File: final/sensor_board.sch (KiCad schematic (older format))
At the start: 47 parts, among them J1 USB_microB_2040002-1, J2 Arduino_ICSP, J3 Conn_01x15_Male, J4 Conn_01x15_Male, J5 BT CONFIG, U1 TXS0104E, U2 FT232RL, U3 RN4871, U4 MCP1702T-5002E_CB, U5 TPS2113ADRBR, U6 US5881, U7 ATMEGA328PB-ANR, Y1 16MHz

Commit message: Fix merge conflicts
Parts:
- added C15, C16: 1µF, Capacitor_SMD:C_0603_1608Metric, symbol Device:C
- added J?: JST-PH Connector, symbol Connector_Generic:Conn_02x02_Odd_Even
- added U7: TS02CQE, Package_DIP:DIP-8_W7.62mm, symbol Analog_Switch:ADG417BN
- added U8: MCP1702T-3302E/CBCT-ND, Package_TO_SOT_SMD:SOT-23, symbol sensor_board-rescue:MCP1702T-5002E_CB-final
- J1: symbol final:USB_microB_2040002-1 -> sensor_board-rescue:USB_microB_2040002-1-final
- J2: symbol final:Arduino_ICSP -> sensor_board-rescue:Arduino_ICSP-final
- S1, S2: symbol final:SW -> sensor_board-rescue:SW-final
- U1: symbol final:TXS0104E -> sensor_board-rescue:TXS0104E-final
- U2: symbol final:FT232RL -> sensor_board-rescue:FT232RL-final
- U4: symbol final:MCP1702T-5002E_CB -> sensor_board-rescue:MCP1702T-5002E_CB-final
- U5: symbol final:TPS2113ADRBR -> sensor_board-rescue:TPS2113ADRBR-final
- U6: symbol final:US5881 -> sensor_board-rescue:US5881-final
- U7: symbol final:ATMEGA328PB-ANR -> main_board-rescue:ATMEGA328PB-ANR-final
- Y1: symbol final:Crystal -> sensor_board-rescue:Crystal-final
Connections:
- net labels added: +3.3V
- wire segments 134 -> 146
- no-connect marks 31 -> 32
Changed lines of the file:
@@
 	4200 1900 4200 1950
-Wire Wire Line
-	4200 1900 3900 1900
-Connection ~ 4200 1900
-Text Label 3900 1900 2    50   ~ 0
-VIN
 Wire Wire Line
 	2200 4600 2400 4600
@@
 	14470 7580 14620 7580
 $Comp
-L final:TPS2113ADRBR U5
+L sensor_board-rescue:TPS2113ADRBR-final U5
 U 1 1 5C6B8D23
 P 7500 2200
@@
 $EndComp
 $Comp
-L final:MCP1702T-5002E_CB U4
+L sensor_board-rescue:MCP1702T-5002E_CB-final U4
 U 1 1 5C6B8EBC
 P 4800 2000
@@
 $EndComp
 $Comp
-L final:SW S2
+L sensor_board-rescue:SW-final S2
 U 1 1 5C6B90CD
 P 7000 5300
@@
 $EndComp
 $Comp
-L final:USB_microB_2040002-1 J1
+L sensor_board-rescue:USB_microB_2040002-1-final J1
 U 1 1 5C6B9394
 P 1550 5000
@@
 $EndComp
 $Comp
-L final:Arduino_ICSP J2
+L sensor_board-rescue:Arduino_ICSP-final J2
 U 1 1 5C6B9A65
 P 14270 7480
@@
 $EndComp
 $Comp
-L final:ATMEGA328PB-ANR U7
+L main_board-rescue:ATMEGA328PB-ANR-final U7
 U 1 1 5C6C352E
 P 9800 6100
@@
 	8650 7800 8650 7850
 $Comp
-L final:FT232RL U2
+L sensor_board-rescue:FT232RL-final U2
 U 1 1 5C6CF653
 P 4500 5500
@@
 $EndComp
 $Comp
-L final:Crystal Y1
+L sensor_board-rescue:Crystal-final Y1
 U 1 1 5C6CF8B9
 P 8500 5200
@@
 $EndComp
 $Comp
-L final:SW S1
+L sensor_board-rescue:SW-final S1
 U 1 1 5CB4A3A3
 P 6710 9320
@@
 	13810 8310 14220 8310
 $Comp
-L final:TXS0104E U1
+L sensor_board-rescue:TXS0104E-final U1
 U 1 1 5CAAB751
 P 2880 9420
@@
 $EndComp
 $Comp
-L final:US5881 U6
+L sensor_board-rescue:US5881-final U6
 U 1 1 5CAB13C9
 P 8450 9120
@@
 Text Label 8800 9120 0    50   ~ 0
 D2
+$Comp
+L power:GND #PWR056
+U 1 1 5CAB55FC
+P 3500 1450
+F 0 "#PWR056" H 3500 1200 50  0001 C CNN
+F 1 "GND" H 3505 1277 50  0000 C CNN
+F 2 "" H 3500 1450 50  0001 C CNN
+F 3 "" H 3500 1450 50  0001 C CNN
+	1    3500 1450
+	1    0    0    -1
+$EndComp
+$Comp
+L Device:C C16
+U 1 1 5CAB5602
+P 4100 1150
+F 0 "C16" H 4215 1196 50  0000 L CNN
+F 1 "1µF" H 4215 1105 50  0000 L CNN
+F 2 "Capacitor_SMD:C_0603_1608Metric" H 4138 1000 50  0001 C CNN
+F 3 "~" H 4100 1150 50  0001 C CNN
+	1    4100 1150
+	1    0    0    -1
+$EndComp
+$Comp
+L power:GND #PWR057
+U 1 1 5CAB5609
+P 4100 1300
+F 0 "#PWR057" H 4100 1050 50  0001 C CNN
+F 1 "GND" H 4105 1127 50  0000 C CNN
+F 2 "" H 4100 1300 50  0001 C CNN
+F 3 "" H 4100 1300 50  0001 C CNN
+	1    4100 1300
+	1    0    0    -1
+$EndComp
+$Comp
+L Device:C C15
+U 1 1 5CAB560F
+P 2900 1150
+F 0 "C15" H 3015 1196 50  0000 L CNN
+F 1 "1µF" H 3015 1105 50  0000 L CNN
+F 2 "Capacitor_SMD:C_0603_1608Metric" H 2938 1000 50  0001 C CNN
+F 3 "~" H 2900 1150 50  0001 C CNN
+	1    2900 1150
+	-1   0    0    -1
+$EndComp
+$Comp
+L power:GND #PWR055
+U 1 1 5CAB5616
+P 2900 1300
+F 0 "#PWR055" H 2900 1050 50  0001 C CNN
+F 1 "GND" H 2905 1127 50  0000 C CNN
+F 2 "" H 2900 1300 50  0001 C CNN
+F 3 "" H 2900 1300 50  0001 C CNN
+	1    2900 1300
+	1    0    0    -1
+$EndComp
+Wire Wire Line
+	4000 950  4100 950
+Wire Wire Line
+	4100 1000 4100 950
+Wire Wire Line
+	3000 950  2900 950
+Wire Wire Line
+	2900 950  2900 1000
+$Comp
+L sensor_board-rescue:MCP1702T-5002E_CB-final U8
+U 1 1 5CAB5626
+P 3500 1050
+F 0 "U8" H 3500 1415 50  0000 C CNN
+F 1 "MCP1702T-3302E/CBCT-ND" H 3500 1324 50  0000 C CNN
+F 2 "Package_TO_SOT_SMD:SOT-23" H 3500 1150 50  0001 C CNN
+F 3 "" H 3500 1150 50  0001 C CNN
+	1    3500 1050
+	1    0    0    -1
+$EndComp
+Wire Wire Line
+	4100 950  4650 950
+Connection ~ 4100 950
+$Comp
+L power:+3.3V #PWR058
+U 1 1 5CAD1AF1
+P 4650 950
+F 0 "#PWR058" H 4650 800 50  0001 C CNN
+F 1 "+3.3V" V 4665 1078 50  0000 L CNN
+F 2 "" H 4650 950 50  0001 C CNN
+F 3 "" H 4650 950 50  0001 C CNN
+	1    4650 950
+	0    1    1    0
+$EndComp
+$Comp
+L Analog_Switch:ADG417BN U7
+U 1 1 5CAD3137
+P 2200 950
+F 0 "U7" H 2200 1217 50  0000 C CNN
+F 1 "TS02CQE" H 2200 1126 50  0000 C CNN
+F 2 "Package_DIP:DIP-8_W7.62mm" H 2200 850 50  0001 C CNN
+F 3 "http://www.analog.com/media/en/technical-documentation/data-sheets/ADG417.pdf" H 2200 950 50  0001 C CNN
+	1    2200 950
+	1    0    0    -1
+$EndComp
+Wire Wire Line
+	2500 950  2550 950
+Connection ~ 2900 950
+NoConn ~ 2200 1150
+Wire Wire Line
+	1900 950  1600 950
+$Comp
+L Connector_Generic:Conn_02x02_Odd_Even J?
+U 1 1 5CB1E020
+P 1300 950
+F 0 "J?" H 1350 1167 50  0000 C CNN
+F 1 "JST-PH Connector" H 1350 1076 50  0000 C CNN
+F 2 "" H 1300 950 50  0001 C CNN
+F 3 "~" H 1300 950 50  0001 C CNN
+	1    1300 950
+	1    0    0    -1
+$EndComp
+$Comp
+L power:GND #PWR?
+U 1 1 5CB1E2D9
+P 1600 1100
+F 0 "#PWR?" H 1600 850 50  0001 C CNN
+F 1 "GND" H 1605 927 50  0000 C CNN
+F 2 "" H 1600 1100 50  0001 C CNN
+F 3 "" H 1600 1100 50  0001 C CNN
+	1    1600 1100
+	1    0    0    -1
+$EndComp
+$Comp
+L power:GND #PWR?
+U 1 1 5CB23E06
+P 1100 1100
+F 0 "#PWR?" H 1100 850 50  0001 C CNN
+F 1 "GND" H 1105 927 50  0000 C CNN
+F 2 "" H 1100 1100 50  0001 C CNN
+F 3 "" H 1100 1100 50  0001 C CNN
+	1    1100 1100
+	1    0    0    -1
+$EndComp
+Wire Wire Line
+	1100 950  800  950
+Text Label 800  950  2    50   ~ 0
+VIN
+Wire Wire Line
+	1100 1050 1100 1100
+Wire Wire Line
+	1600 1050 1600 1100
+Wire Wire Line
+	2550 950  2550 1900
+Wire Wire Line
+	2550 1900 4200 1900
+Connection ~ 2550 950
+Wire Wire Line
+	2550 950  2900 950
+Connection ~ 4200 1900
 $EndSCHEMATC

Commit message: Add diode to 3V3 output of FTDI and power display from Lin Reg.
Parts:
- added D?: D_Schottky, symbol Device:D_Schottky
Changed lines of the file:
@@
 L power:+3V3 #PWR08
 U 1 1 5C4E2E65
-P 3300 6800
-F 0 "#PWR08" H 3300 6650 50  0001 C CNN
-F 1 "+3V3" V 3315 6928 50  0000 L CNN
-F 2 "" H 3300 6800 50  0001 C CNN
-F 3 "" H 3300 6800 50  0001 C CNN
-	1    3300 6800
+P 3000 6800
+F 0 "#PWR08" H 3000 6650 50  0001 C CNN
+F 1 "+3V3" V 3015 6928 50  0000 L CNN
+F 2 "" H 3000 6800 50  0001 C CNN
+F 3 "" H 3000 6800 50  0001 C CNN
+	1    3000 6800
 	0    -1   -1   0
 $EndComp
@@
 NoConn ~ 3330 9670
 $Comp
-L power:+3V3 #PWR06
-U 1 1 5CADBD7A
-P 2980 8340
-F 0 "#PWR06" H 2980 8190 50  0001 C CNN
-F 1 "+3V3" V 2980 8490 50  0000 L CNN
-F 2 "" H 2980 8340 50  0001 C CNN
-F 3 "" H 2980 8340 50  0001 C CNN
-	1    2980 8340
-	-1   0    0    -1
-$EndComp
-$Comp
 L power:+5V #PWR04
 U 1 1 5CADBE18
@@
 	2550 950  2900 950
 Connection ~ 4200 1900
+$Comp
+L Device:D_Schottky D?
+U 1 1 5CAC01BF
+P 3150 6800
+F 0 "D?" H 3150 7016 50  0000 C CNN
+F 1 "D_Schottky" H 3150 6925 50  0000 C CNN
+F 2 "" H 3150 6800 50  0001 C CNN
+F 3 "~" H 3150 6800 50  0001 C CNN
+	1    3150 6800
+	1    0    0    -1
+$EndComp
+$Comp
+L power:+3.3V #PWR?
+U 1 1 5CAC1029
+P 2980 8340
+F 0 "#PWR?" H 2980 8190 50  0001 C CNN
+F 1 "+3.3V" V 2995 8468 50  0000 L CNN
+F 2 "" H 2980 8340 50  0001 C CNN
+F 3 "" H 2980 8340 50  0001 C CNN
+	1    2980 8340
+	1    0    0    -1
+$EndComp
 $EndSCHEMATC

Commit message: Hook up reset on BT to MCU
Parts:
- gave numbers to parts that had none: 2
- renumbered C8 to C10, C9 to C11, C10 to C12, C11 to C13, C12 to C14, C13 to C15, C14 to C16, C15 to C2, C2 to C3, C3 to C4, C4 to C5, C5 to C6, C16 to C7, C6 to C8, C7 to C9, D1 to D2, D2 to D3, D3 to D4, D4 to D5, D5 to D6, J1 to J2, J2 to J3, J3 to J4, J4 to J5, J5 to J6, U7 to U1, U1 to U2, U8 to U3, U2 to U4, U3 to U5, U4 to U6, U5 to U7, U6 to U8, U7 to U9
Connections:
- no-connect marks 32 -> 30

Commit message: Added Power Schematic
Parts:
- removed C1, C14, C15, C16, C3, C5: 0.1µF, Capacitor_SMD:C_0603_1608Metric, symbol Device:C
- removed C10: 10µF, Capacitor_SMD:C_0805_2012Metric, symbol Device:C
- removed C8, C9: 1µF, Capacitor_SMD:C_0603_1608Metric, symbol Device:C
- removed D1: D_Schottky, symbol Device:D_Schottky
- removed D2: BTPWR, symbol Device:LED
- removed J3: Arduino_ICSP, mp3b:Arduino_ICSP, symbol sensor_board-rescue:Arduino_ICSP-final
- removed R1: 47K, symbol Device:R
- removed R13, R2, R6: 1K, Resistor_SMD:R_0603_1608Metric, symbol Device:R
- removed R3, R9: 1K, symbol Device:R
- removed R8: 20K, Resistor_SMD:R_0603_1608Metric, symbol Device:R
- removed S2: SW, Button_Switch_SMD:SW_SPST_B3U-1000P, symbol sensor_board-rescue:SW-final
- removed U4: FT232RL, symbol sensor_board-rescue:FT232RL-final
- removed U6: MCP1702T-5002E_CB, Package_TO_SOT_SMD:SOT-23, symbol sensor_board-rescue:MCP1702T-5002E_CB-final
- removed U7: TPS2113ADRBR, symbol sensor_board-rescue:TPS2113ADRBR-final
- removed U9: ATMEGA328PB-ANR, symbol main_board-rescue:ATMEGA328PB-ANR-final
- removed Y1: 16MHz, mp3b:CSTNE, symbol sensor_board-rescue:Crystal-final
- added C? (x6): 0.1µF, Capacitor_SMD:C_0603_1608Metric, symbol Device:C
- added C? (x4): 1µF, Capacitor_SMD:C_0603_1608Metric, symbol Device:C
- added C?: 10µF, Capacitor_SMD:C_0805_2012Metric, symbol Device:C
- added C? (x2): 10µF, Capacitor_SMD:C_0603_1608Metric, symbol Device:C
- added D?: BTPWR, symbol Device:LED
- added D?: LED, LED_SMD:LED_0805_2012Metric, symbol Device:LED_ALT
- added J?: Arduino_ICSP, mp3b:Arduino_ICSP, symbol sensor_board-rescue:Arduino_ICSP-final
- added R? (x4): 1K, Resistor_SMD:R_0603_1608Metric, symbol Device:R
- added R?: 20K, Resistor_SMD:R_0603_1608Metric, symbol Device:R
- added R?: 47K, symbol Device:R
- added R? (x2): 1K, symbol Device:R
- added R?: 590, Resistor_SMD:R_0603_1608Metric, symbol Device:R
- added R?: 1.1k, Resistor_SMD:R_0603_1608Metric, symbol Device:R
- added R?: 100k, Resistor_SMD:R_0603_1608Metric, symbol Device:R
- added R? (x3): 10k, Resistor_SMD:R_0603_1608Metric, symbol Device:R
- added R?: .01, Resistor_SMD:R_0603_1608Metric, symbol Device:R
- added R? (x2): 4.7k, Resistor_SMD:R_0603_1608Metric, symbol Device:R
- added S?: SW, Button_Switch_SMD:SW_SPST_B3U-1000P, symbol sensor_board-rescue:SW-final
- added U?: TPS2113ADRBR, symbol sensor_board-rescue:TPS2113ADRBR-final
- added U?: MCP1702T-5002E_CB, Package_TO_SOT_SMD:SOT-23, symbol sensor_board-rescue:MCP1702T-5002E_CB-final
- added U?: ATMEGA328PB-ANR, symbol main_board-rescue:ATMEGA328PB-ANR-final
- added U?: FT232RL, symbol sensor_board-rescue:FT232RL-final
- added U?: BQ24075, symbol Battery_Management:BQ24075
- added U?: BQ27441-G1, Package_SON:Texas_S-PDSO-N12, symbol Battery_Management:BQ27441-G1
- added Y?: 16MHz, mp3b:CSTNE, symbol sensor_board-rescue:Crystal-final
- renumbered C13 to C?, C6 to C?, C11 to C?, C4 to C?, C12 to C?, C7 to C?, C2 to C?, D5 to D?, D3 to D?, D4 to D?, D6 to D?, J4 to J?, J5 to J?, J2 to J?, J1 to J?, J6 to J?, R4 to R?, R7 to R?, R11 to R?, R5 to R?, R10 to R?, R12 to R?, S1 to S?, U2 to U?, U8 to U?, U3 to U?, U1 to U?, U5 to U?
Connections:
- net labels added: BATTERY, OUT, VPU, V_BATT
- wire segments 146 -> 216
- no-connect marks 30 -> 38
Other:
- moved on the sheet: C?, D?, J?, R?, S?, U?

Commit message: Update Power 4/11
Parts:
- removed D?: LED, LED_SMD:LED_0805_2012Metric, symbol Device:LED_ALT
- removed J?: JST-PH Connector, symbol Connector_Generic:Conn_02x02_Odd_Even
- removed R?: 1K, Resistor_SMD:R_0603_1608Metric, symbol Device:R
- removed U?: TS02CQE, Package_DIP:DIP-8_W7.62mm, symbol Analog_Switch:ADG417BN
- added C21: 0.47µF, Capacitor_SMD:C_0603_1608Metric, symbol Device:C
- added D6: LED, LED_SMD:LED_0805_2012Metric, symbol Device:LED_ALT
- added J4: Conn_01x02_Male, symbol Connector:Conn_01x02_Male
- added R19: 1K, Resistor_SMD:R_0603_1608Metric, symbol Device:R
- added R24: 10k, Resistor_SMD:R_0603_1608Metric, symbol Device:R
- added SW?: SW_DIP_x01, symbol Switch:SW_DIP_x01
- gave numbers to parts that had none: 65
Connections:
- net labels removed: OUT, VPU
- wire segments 216 -> 219
- no-connect marks 38 -> 37
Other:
- moved on the sheet: C18, C19, C20, J3, J5, J6, J7, R20, R21, R22, R23, U11

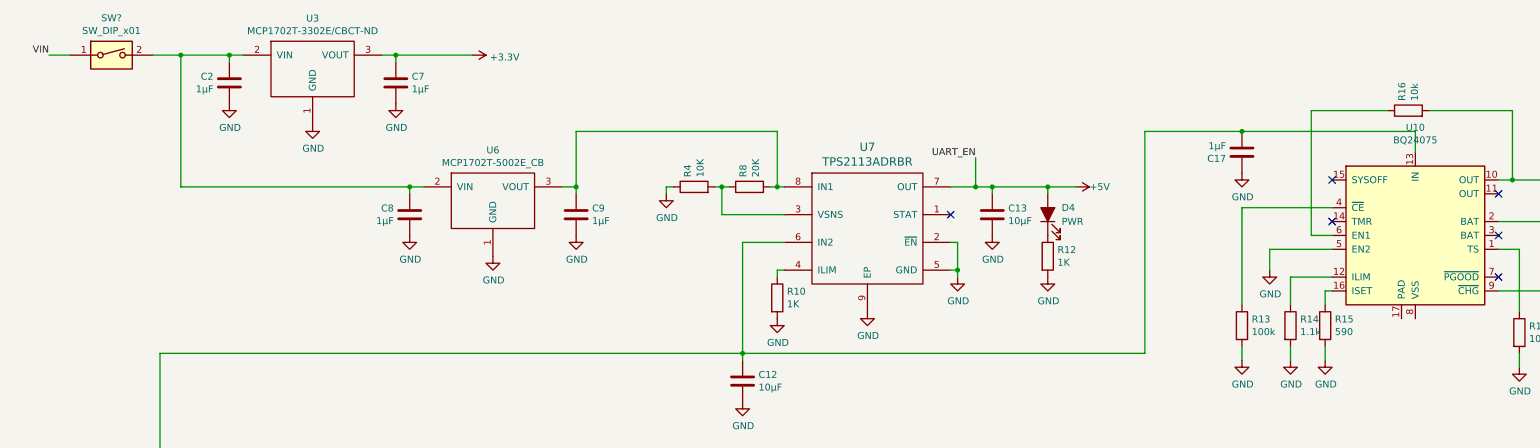
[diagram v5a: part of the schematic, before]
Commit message: Ground pins
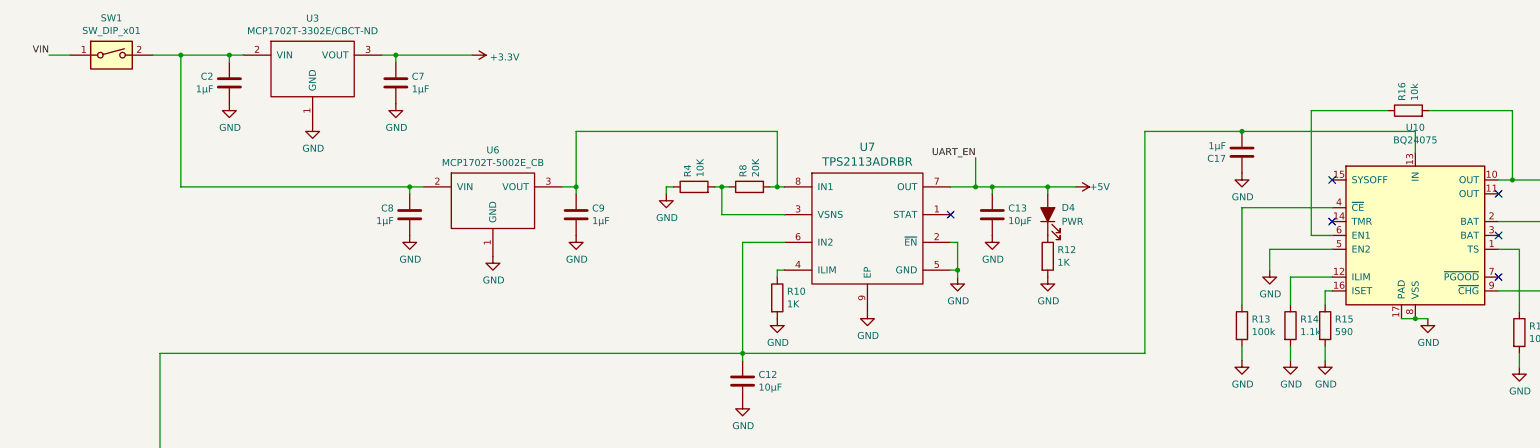
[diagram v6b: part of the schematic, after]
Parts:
- gave numbers to parts that had none: 1
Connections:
- net GND: now also U10.17 (PAD), U10.8 (VSS)
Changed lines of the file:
@@
 A5
 $Comp
-L Switch:SW_DIP_x01 SW?
+L Switch:SW_DIP_x01 SW1
 U 1 1 5CE2D004
 P 2200 1050
-F 0 "SW?" H 2200 1317 50  0000 C CNN
+F 0 "SW1" H 2200 1317 50  0000 C CNN
 F 1 "SW_DIP_x01" H 2200 1226 50  0000 C CNN
 F 2 "" H 2200 1050 50  0001 C CNN
@@
 Wire Wire Line
 	14800 2150 14800 1850
+$Comp
+L power:GND #PWR0102
+U 1 1 5CB0332E
+P 11690 2950
+F 0 "#PWR0102" H 11690 2700 50  0001 C CNN
+F 1 "GND" H 11695 2777 50  0000 C CNN
+F 2 "" H 11690 2950 50  0001 C CNN
+F 3 "" H 11690 2950 50  0001 C CNN
+	1    11690 2950
+	1    0    0    -1
+$EndComp
+Wire Wire Line
+	11600 2950 11690 2950
+Wire Wire Line
+	11500 2950 11600 2950
+Connection ~ 11600 2950
 $EndSCHEMATC

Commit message: Made Boards Better
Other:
- note added: "Battery Gauge"
- note added: "Battery Header"
- note added: "Battery Multiplexer + Charger"
- moved on the sheet: D6, J3, J4, J5, J6, J7, R19
